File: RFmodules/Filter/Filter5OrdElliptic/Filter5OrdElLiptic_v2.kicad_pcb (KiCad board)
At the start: 2 copper layers, 39.1 x 13.2 mm, 17 parts, among them J1 SMA, J2 SMA

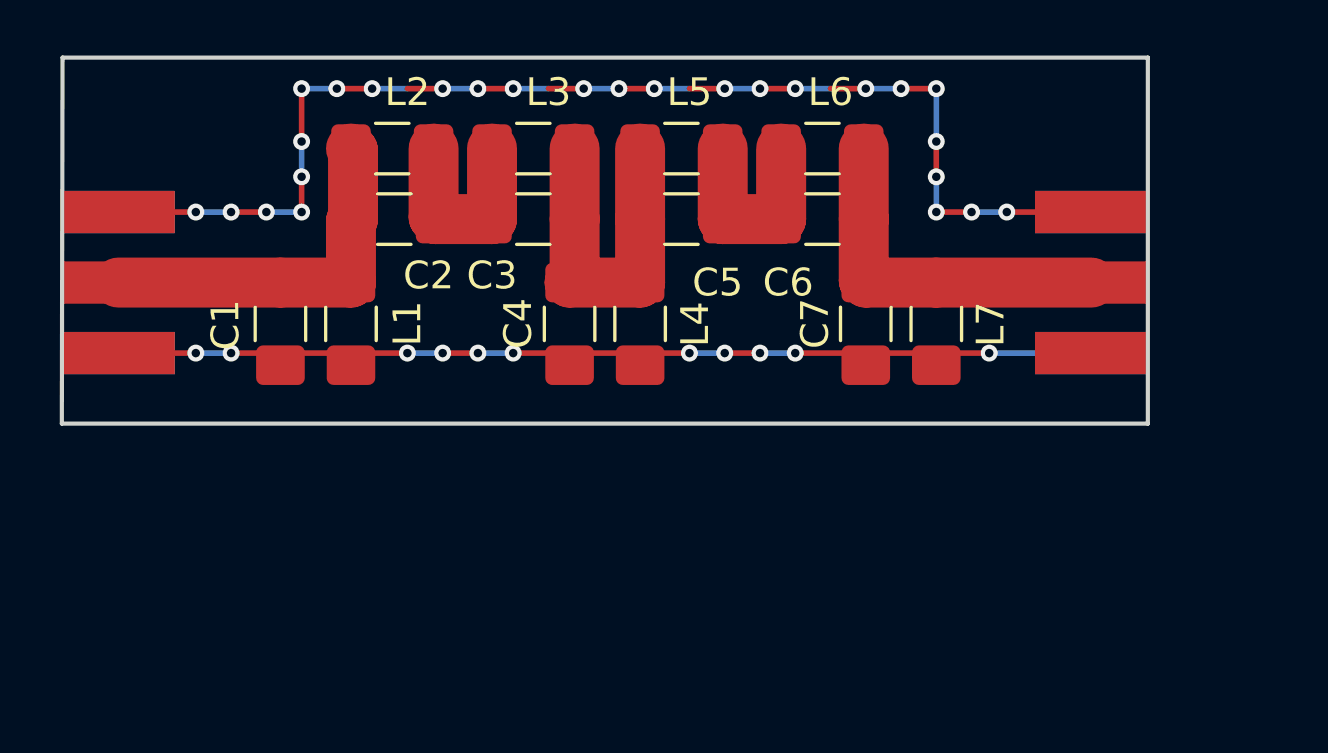
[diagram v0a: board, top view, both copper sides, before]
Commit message: Fix design guide issues and typos
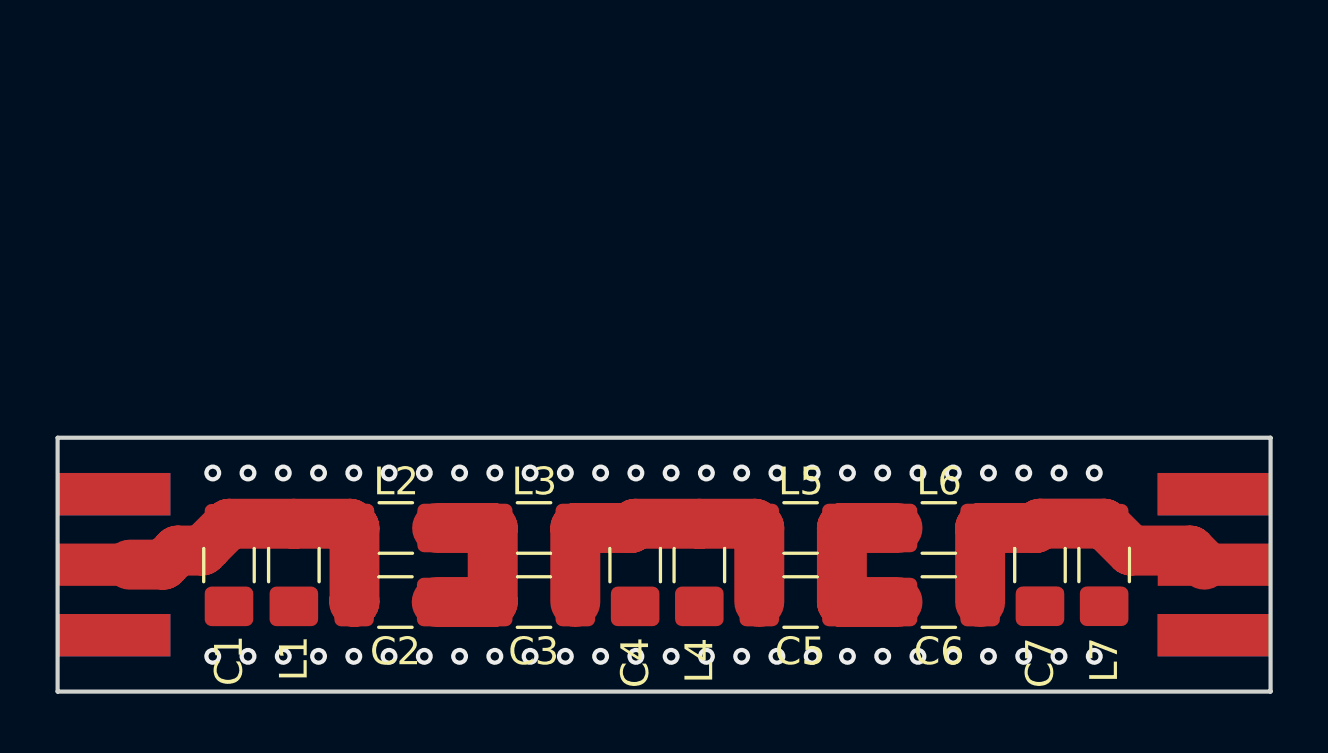
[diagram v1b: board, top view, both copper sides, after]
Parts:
- removed J1, J2: SMA, RFLego_Footprint:SMA_Edge
- added IN: SMA, RFLego_Footprint:SMA_Edge, F.Cu at (99.4, 90.2)
- added OUT: SMA, RFLego_Footprint:SMA_Edge, F.Cu at (139.0, 90.2)
- moved C5 14.4 mm to (126.2, 91.5)
- moved C6 14.4 mm to (131.2, 91.5)
- moved L5 14.3 mm to (126.2, 88.8)
- moved L6 14.3 mm to (131.2, 88.8)
- moved C2 13.8 mm to (111.6, 91.5)
- moved C3 13.8 mm to (116.6, 91.5)
- moved L2 13.7 mm to (111.6, 88.8)
- moved L3 13.7 mm to (116.6, 88.8)
- moved C7 10.7 mm to (134.8, 90.2)
- moved L7 10.6 mm to (137.1, 90.2)
- moved C4 9.00 mm to (120.2, 90.2)
- moved L4 8.94 mm to (122.5, 90.2)
- moved L1 8.93 mm to (107.9, 90.2)
- moved C1 8.88 mm to (105.6, 90.2)
- moved REF** 8.81 mm to (107.1, 90.1)
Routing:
- net GND: track 79.0 -> 0.00 mm, vias 37 -> 52
- net Net-(C1-Pad1): track 13.3 -> 11.4 mm
- net Net-(C6-Pad1): track 13.0 -> 11.4 mm
- net Net-(C5-Pad1): track 7.19 -> 6.67 mm
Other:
- board size 39.1 x 13.2 mm -> 43.7 x 9.1 mm

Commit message: Update board descriptions, add Bandstop elliptic filter 5th order
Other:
- board text added: "Bandpass Filter Elliptic 5th Order Revision 1 - 01/2019 github.com/fgaletsee/RFLego"
- board text removed: "Bandpass Filter Elliptic 5th Order Revision 0.1.0 - 01/2019 github.com/fgaletsee/RFLego"
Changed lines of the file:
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@@
       (xy -2.549664 -1.91989) (xy -2.469928 -1.911165) (xy -2.400256 -1.919918)) (layer B.SilkS) (width 0.01))
   )
-  (gr_text "Bandpass Filter Elliptic 5th Order\nRevision 0.1.0 - 01/2019\ngithub.com/fgaletsee/RFLego\n" (at 138.43 89.1794) (layer B.SilkS)
+  (gr_text "Bandpass Filter Elliptic 5th Order\nRevision 1 - 01/2019\ngithub.com/fgaletsee/RFLego\n" (at 138.43 89.1794) (layer B.SilkS)
     (effects (font (size 0.75 0.75) (thickness 0.1875)) (justify left mirror))
   )
